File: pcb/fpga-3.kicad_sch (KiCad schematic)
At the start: 6 parts, among them U5 XC7A100T-FGG484, Y1 SiT9365AI-2B2-33E200.000000

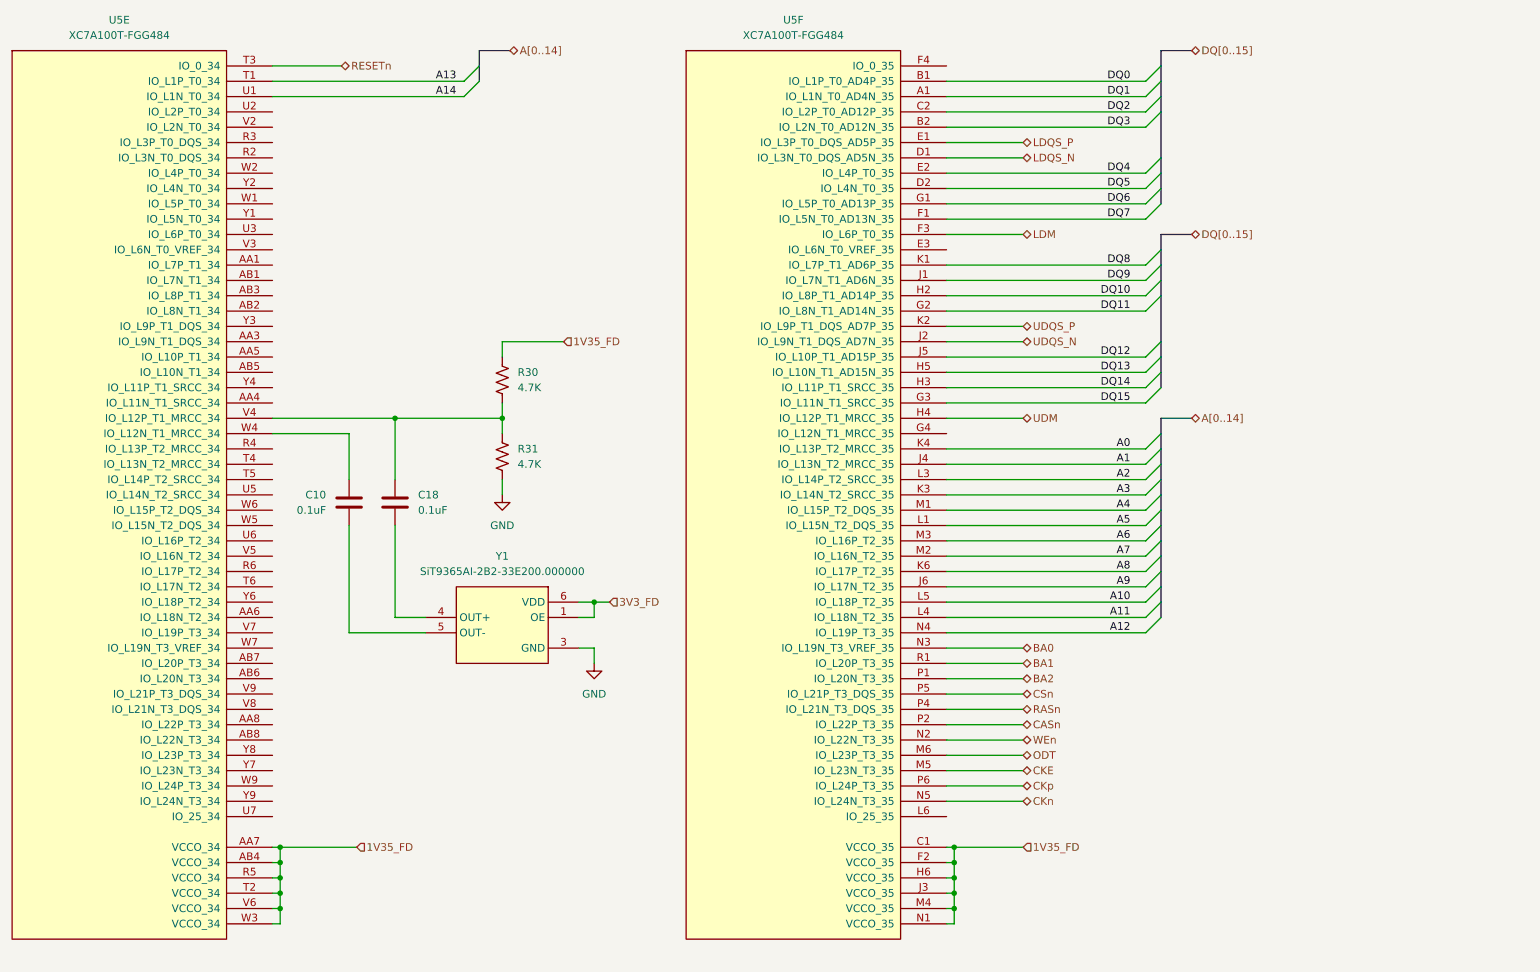
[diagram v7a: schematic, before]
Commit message: moved stuff around, bom
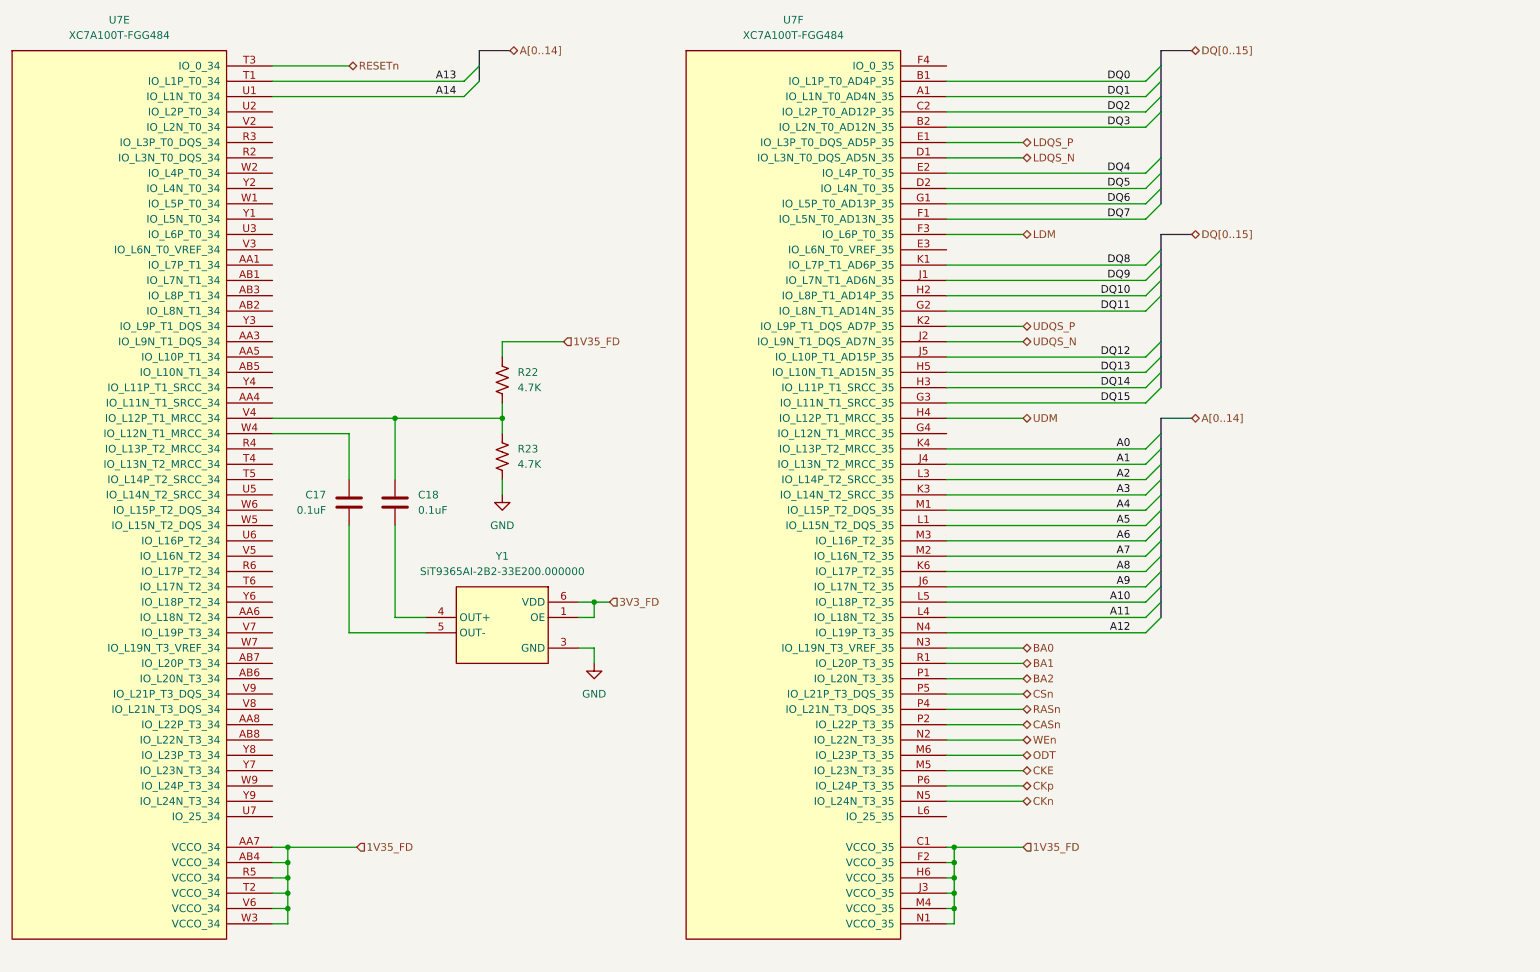
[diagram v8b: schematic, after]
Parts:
- renumbered C10 to C17, R30 to R22, R31 to R23, U5 to U7
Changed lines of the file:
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@@
 	)
 	(junction
-		(at 62.23 165.1)
+		(at 63.5 165.1)
 		(diameter 0)
 		(color 0 0 0 0)
@@
 	)
 	(junction
-		(at 62.23 160.02)
+		(at 63.5 160.02)
 		(diameter 0)
 		(color 0 0 0 0)
@@
 	)
 	(junction
-		(at 62.23 162.56)
+		(at 63.5 162.56)
 		(diameter 0)
 		(color 0 0 0 0)
 	)
 	(junction
-		(at 62.23 157.48)
+		(at 63.5 157.48)
 		(diameter 0)
 		(color 0 0 0 0)
@@
 	)
 	(junction
-		(at 62.23 154.94)
+		(at 63.5 154.94)
 		(diameter 0)
 		(color 0 0 0 0)
@@
 	(wire
 		(pts
+			(xy 60.96 160.02) (xy 63.5 160.02)
+		)
+		(stroke
+			(width 0)
+			(type default)
+		)
+	)
+	(wire
+		(pts
 			(xy 114.3 114.3) (xy 114.3 116.84)
 		)
@@
 	(wire
 		(pts
+			(xy 60.96 154.94) (xy 63.5 154.94)
+		)
+		(stroke
+			(width 0)
+			(type default)
+		)
+	)
+	(wire
+		(pts
 			(xy 172.72 33.02) (xy 205.74 33.02)
 		)
@@
 	(wire
 		(pts
-			(xy 60.96 25.4) (xy 72.39 25.4)
+			(xy 60.96 25.4) (xy 73.66 25.4)
 		)
 		(stroke
@@
 	(wire
 		(pts
-			(xy 62.23 154.94) (xy 60.96 154.94)
-		)
-		(stroke
-			(width 0)
-			(type default)
-		)
-	)
-	(wire
-		(pts
 			(xy 172.72 43.18) (xy 205.74 43.18)
 		)
@@
 	(wire
 		(pts
-			(xy 62.23 157.48) (xy 60.96 157.48)
-		)
-		(stroke
-			(width 0)
-			(type default)
-		)
-	)
-	(wire
-		(pts
 			(xy 172.72 104.14) (xy 205.74 104.14)
 		)
@@
 	(wire
 		(pts
-			(xy 62.23 160.02) (xy 60.96 160.02)
-		)
-		(stroke
-			(width 0)
-			(type default)
-		)
-	)
-	(wire
-		(pts
-			(xy 62.23 165.1) (xy 62.23 167.64)
-		)
-		(stroke
-			(width 0)
-			(type default)
-		)
-	)
-	(wire
-		(pts
-			(xy 62.23 165.1) (xy 60.96 165.1)
+			(xy 63.5 165.1) (xy 63.5 167.64)
 		)
 		(stroke
@@
 	(wire
 		(pts
-			(xy 172.72 139.7) (xy 185.42 139.7)
+			(xy 60.96 165.1) (xy 63.5 165.1)
 		)
 		(stroke
@@
 	(wire
 		(pts
-			(xy 172.72 116.84) (xy 205.74 116.84)
+			(xy 172.72 139.7) (xy 185.42 139.7)
 		)
 		(stroke
@@
 	(wire
 		(pts
-			(xy 114.3 114.3) (xy 111.76 114.3)
+			(xy 172.72 116.84) (xy 205.74 116.84)
 		)
 		(stroke
@@
 	(wire
 		(pts
-			(xy 173.99 162.56) (xy 172.72 162.56)
+			(xy 114.3 114.3) (xy 111.76 114.3)
 		)
 		(stroke
@@
 	(wire
 		(pts
-			(xy 73.66 86.36) (xy 60.96 86.36)
+			(xy 173.99 162.56) (xy 172.72 162.56)
 		)
 		(stroke
@@
 	(wire
 		(pts
-			(xy 62.23 167.64) (xy 60.96 167.64)
+			(xy 73.66 86.36) (xy 60.96 86.36)
 		)
 		(stroke
@@
 		)
 	)
+	(wire
+		(pts
+			(xy 60.96 157.48) (xy 63.5 157.48)
+		)
+		(stroke
+			(width 0)
+			(type default)
+		)
+	)
 	(bus
 		(pts
@@
 	(wire
 		(pts
-			(xy 62.23 154.94) (xy 62.23 157.48)
+			(xy 63.5 154.94) (xy 63.5 157.48)
 		)
 		(stroke
@@
 	(wire
 		(pts
+			(xy 60.96 162.56) (xy 63.5 162.56)
+		)
+		(stroke
+			(width 0)
+			(type default)
+		)
+	)
+	(wire
+		(pts
 			(xy 173.99 154.94) (xy 172.72 154.94)
 		)
@@
 	(wire
 		(pts
-			(xy 62.23 160.02) (xy 62.23 162.56)
+			(xy 63.5 160.02) (xy 63.5 162.56)
 		)
 		(stroke
@@
 	(wire
 		(pts
-			(xy 62.23 154.94) (xy 74.93 154.94)
+			(xy 63.5 154.94) (xy 74.93 154.94)
 		)
 		(stroke
@@
 	(wire
 		(pts
-			(xy 62.23 162.56) (xy 60.96 162.56)
-		)
-		(stroke
-			(width 0)
-			(type default)
-		)
-	)
-	(wire
-		(pts
-			(xy 62.23 162.56) (xy 62.23 165.1)
+			(xy 63.5 162.56) (xy 63.5 165.1)
 		)
 		(stroke
@@
 	(wire
 		(pts
-			(xy 62.23 157.48) (xy 62.23 160.02)
+			(xy 60.96 167.64) (xy 63.5 167.64)
+		)
+		(stroke
+			(width 0)
+			(type default)
+		)
+	)
+	(wire
+		(pts
+			(xy 63.5 157.48) (xy 63.5 160.02)
 		)
 		(stroke
@@
 	(hierarchical_label "RESETn"
 		(shape bidirectional)
-		(at 72.39 25.4 0)
+		(at 73.66 25.4 0)
 		(effects
 			(font
@@
 		(dnp no)
 		(fields_autoplaced yes)
-		(property "Reference" "U5"
+		(property "Reference" "U7"
 			(at 147.32 17.78 0)
 			(effects
@@
 			(project "RPi-HwAB-1"
 				(path "/e63e39d7-6ac0-4ffd-8aa3-1841a4541b55/59d21473-a004-4514-8090-fd93db818925/143e814b-c088-43b0-8f2f-ada8c438e494"
-					(reference "U5")
+					(reference "U7")
 					(unit 6)
 				)
@@
 		(dnp no)
 		(fields_autoplaced yes)
-		(property "Reference" "U5"
+		(property "Reference" "U7"
 			(at 35.56 17.78 0)
 			(effects
@@
 			(project "RPi-HwAB-1"
 				(path "/e63e39d7-6ac0-4ffd-8aa3-1841a4541b55/59d21473-a004-4514-8090-fd93db818925/143e814b-c088-43b0-8f2f-ada8c438e494"
-					(reference "U5")
+					(reference "U7")
 					(unit 5)
 				)
@@
 		(dnp no)
 		(fields_autoplaced yes)
-		(property "Reference" "R30"
+		(property "Reference" "R22"
 			(at 101.6 76.1999 0)
 			(effects
@@
 			(project "RPi-HwAB-1"
 				(path "/e63e39d7-6ac0-4ffd-8aa3-1841a4541b55/59d21473-a004-4514-8090-fd93db818925/143e814b-c088-43b0-8f2f-ada8c438e494"
-					(reference "R30")
+					(reference "R22")
 					(unit 1)
 				)
@@
 		(dnp no)
 		(fields_autoplaced yes)
-		(property "Reference" "R31"
+		(property "Reference" "R23"
 			(at 101.6 88.8999 0)
 			(effects
@@
 			(project "RPi-HwAB-1"
 				(path "/e63e39d7-6ac0-4ffd-8aa3-1841a4541b55/59d21473-a004-4514-8090-fd93db818925/143e814b-c088-43b0-8f2f-ada8c438e494"
-					(reference "R31")
+					(reference "R23")
 					(unit 1)
 				)
@@
 		(dnp no)
 		(fields_autoplaced yes)
-		(property "Reference" "#PWR038"
+		(property "Reference" "#PWR023"
 			(at 99.06 102.87 0)
 			(effects
@@
 			(project "RPi-HwAB-1"
 				(path "/e63e39d7-6ac0-4ffd-8aa3-1841a4541b55/59d21473-a004-4514-8090-fd93db818925/143e814b-c088-43b0-8f2f-ada8c438e494"
-					(reference "#PWR038")
+					(reference "#PWR023")
 					(unit 1)
 				)
@@
 		(dnp no)
 		(fields_autoplaced yes)
-		(property "Reference" "#PWR023"
+		(property "Reference" "#PWR024"
 			(at 114.3 130.81 0)
 			(effects
@@
 			(project ""
 				(path "/e63e39d7-6ac0-4ffd-8aa3-1841a4541b55/59d21473-a004-4514-8090-fd93db818925/143e814b-c088-43b0-8f2f-ada8c438e494"
-					(reference "#PWR023")
+					(reference "#PWR024")
 					(unit 1)
 				)
@@
 		(on_board yes)
 		(dnp no)
-		(property "Reference" "C10"
+		(property "Reference" "C17"
 			(at 69.85 96.52 0)
 			(effects
@@
 			(project "RPi-HwAB-1"
 				(path "/e63e39d7-6ac0-4ffd-8aa3-1841a4541b55/59d21473-a004-4514-8090-fd93db818925/143e814b-c088-43b0-8f2f-ada8c438e494"
-					(reference "C10")
+					(reference "C17")
 					(unit 1)
 				)
